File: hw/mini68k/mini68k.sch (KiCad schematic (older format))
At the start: 27 parts, among them J1 Jack-DC, J2 FTDI header, SW1 SW_SPDT, SW2 SW_Push, U1 HM62256BLP-7, U2 68008D, U3 L7805, U4 28C256, U5 GAL16V8, U6 74LS05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

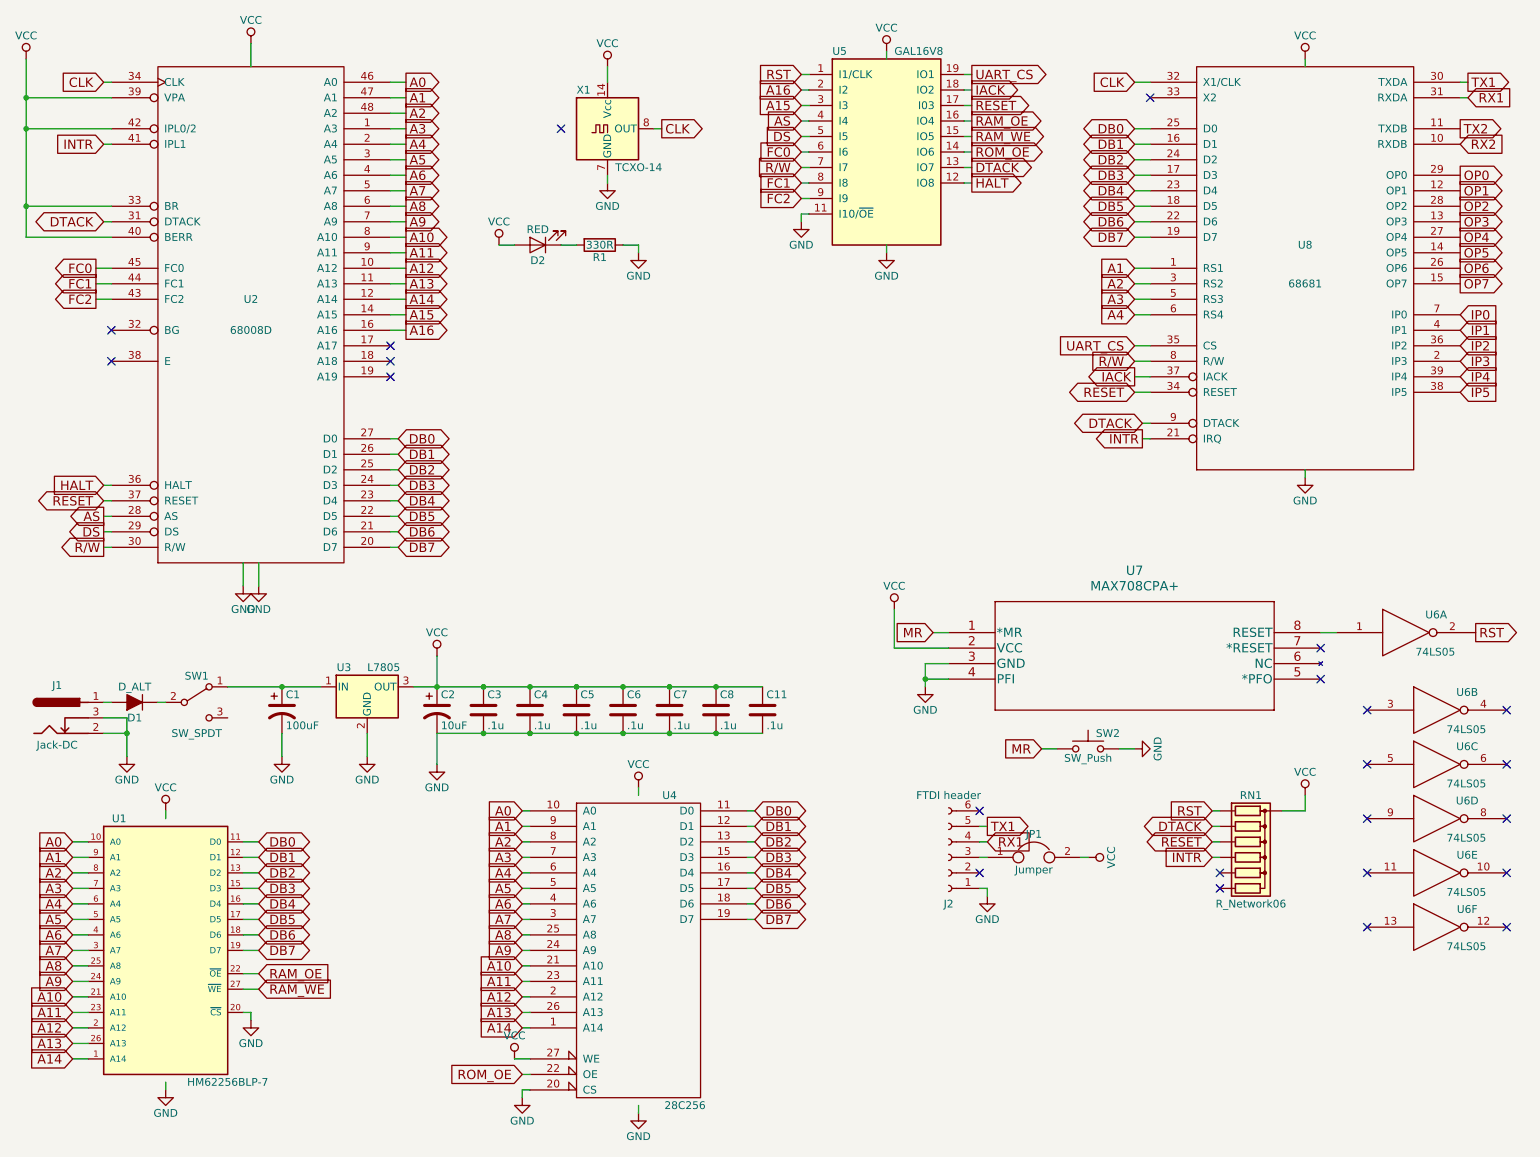
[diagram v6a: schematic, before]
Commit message: update footprints, expose i/o from 68681
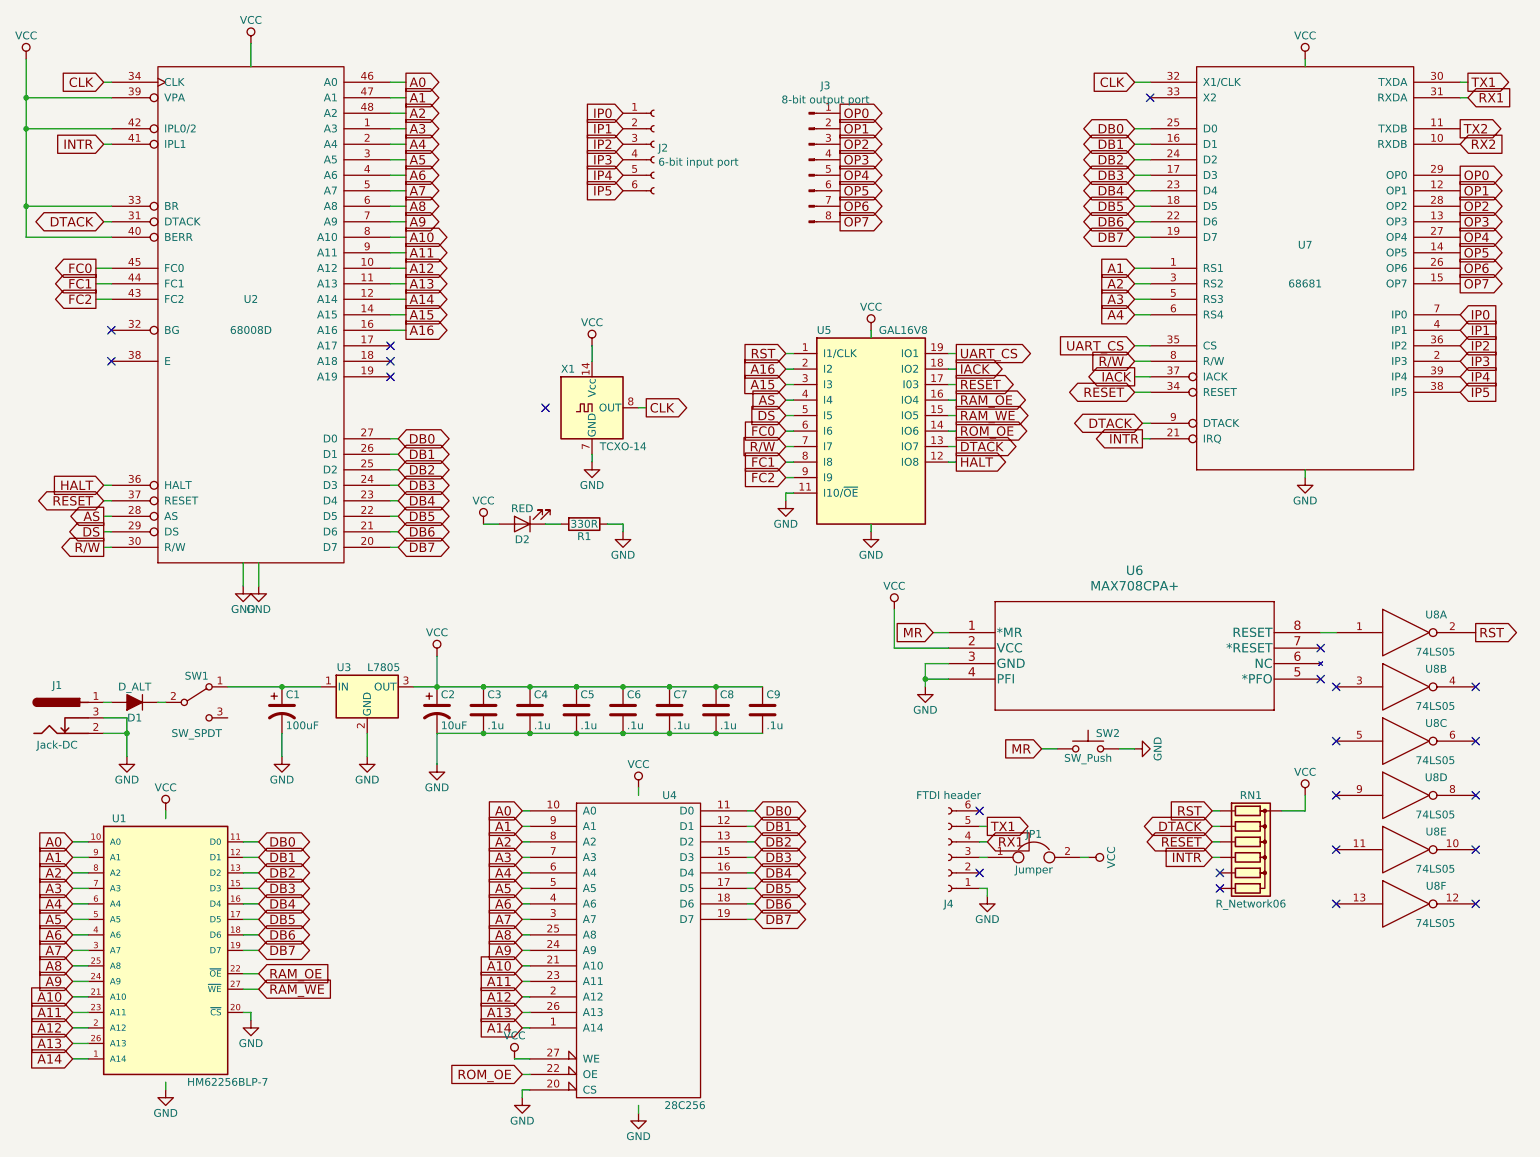
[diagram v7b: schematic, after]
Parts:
- added J2: 6-bit input port, Connector_PinHeader_2.54mm:PinHeader_1x06_P2.54mm_Vertical, symbol Connector:Conn_01x06_Female
- added J3: 8-bit output port, Connector_PinHeader_2.54mm:PinHeader_1x08_P2.54mm_Vertical, symbol Connector:Conn_01x08_Male
- C3, C4, C5, C6, C7, C8: footprint Capacitors_THT:C_Disc_D5.0mm_W2.5mm_P2.50mm -> Capacitor_THT:C_Disc_D5.0mm_W2.5mm_P2.50mm
- C9: renamed from C11; footprint Capacitors_THT:C_Disc_D5.0mm_W2.5mm_P2.50mm -> Capacitor_THT:C_Disc_D5.0mm_W2.5mm_P2.50mm
- J4: renamed from J2; footprint Pin_Headers:Pin_Header_Straight_1x06_Pitch2.54mm -> Connector_PinHeader_2.54mm:PinHeader_1x06_P2.54mm_Vertical
- U1, U4: footprint Housings_DIP:DIP-28_W15.24mm_LongPads -> Package_DIP:DIP-28_W15.24mm_LongPads
- U2: footprint Housings_DIP:DIP-48_W15.24mm_LongPads -> Package_DIP:DIP-48_W15.24mm_LongPads
- U5: footprint Housings_DIP:DIP-20_W7.62mm_LongPads -> Package_DIP:DIP-20_W7.62mm_LongPads
- U6: renamed from U7; footprint Housings_DIP:DIP-8_W7.62mm_LongPads -> Package_DIP:DIP-8_W7.62mm_LongPads
- U7: renamed from U8; footprint Housings_DIP:DIP-40_W15.24mm_LongPads -> Package_DIP:DIP-40_W15.24mm_LongPads
- U8: renamed from U6; footprint Housings_DIP:DIP-14_W7.62mm_LongPads -> Package_DIP:DIP-14_W7.62mm_LongPads
- U8: renamed from U6; footprint (none) -> Package_DIP:DIP-14_W7.62mm_LongPads
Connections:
- net IP0: now also J2.1 (Pin_1)
- net IP1: now also J2.2 (Pin_2)
- net IP2: now also J2.3 (Pin_3)
- net IP3: now also J2.4 (Pin_4)
- net IP4: now also J2.5 (Pin_5)
- net IP5: now also J2.6 (Pin_6)
- net OP0: now also J3.1 (Pin_1)
- net OP1: now also J3.2 (Pin_2)
- net OP2: now also J3.3 (Pin_3)
- net OP3: now also J3.4 (Pin_4)
- net OP4: now also J3.5 (Pin_5)
- net OP5: now also J3.6 (Pin_6)
- net OP6: now also J3.7 (Pin_7)
- net OP7: now also J3.8 (Pin_8)
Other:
- moved on the sheet: D2, R1, U5, U8B, U8C, U8D, U8E, U8F, X1

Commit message: better fills
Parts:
- added J5: FTDI header COM2, Connector_PinHeader_2.54mm:PinHeader_1x06_P2.54mm_Vertical, symbol mini68k-rescue:Conn_01x06_Female
- added JP2: Jumper, Connector_PinHeader_2.54mm:PinHeader_1x02_P2.54mm_Vertical, symbol Device:Jumper
- J4: value FTDI header -> FTDI header COM1
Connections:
- net GND: now also J5.1 (Pin_1)
- net RX2: now also J5.4 (Pin_4)
- net TX2: now also J5.5 (Pin_5)
- net VCC: now also JP2.2
- new net: J5.3 (Pin_3), JP2.1
- no-connect marks 23 -> 25
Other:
- moved on the sheet: D2, J2, J3, J4, JP1, R1, X1
